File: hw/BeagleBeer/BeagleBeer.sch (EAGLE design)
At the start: 104 parts, among them Q10 BSS138, Q9 BSS138, U1 TEMPERATURE-SENSORUMAX8, U4 CAT24C256WI-GT3, U5 BEAGLEBONE_OUTLINEBEAGLEBEER

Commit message: BeagleBeer v2 Run ERCs and DRCs
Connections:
- new net N$12: JP2.20, U5.GPIO2_13
- new net N$13: JP2.21, U5.GPIO2_11
- new net N$20: JP1.4, U5.GPIO2_12
- new net N$21: JP1.3, U5.GPIO2_10
- net 3.3V: now also R15.2, R16.2, R22.2, R25.2
- net LED_FLOW_B_3P3: now also U2.A2
- net LED_FLOW_C_3P3: no longer JP2.20, U5.GPIO2_13
- net LED_FLOW_D_3P3: no longer JP2.21, U5.GPIO2_11
- net N$2: now also JP1.2, U5.GPIO2_8; no longer R22.2, R25.2
- net N$3: now also JP1.1, U5.GPIO2_6; no longer R15.2, R16.2
- net RELAY_A_3P3: no longer JP1.4, U5.GPIO2_12
- net RELAY_B_3P3: no longer JP1.3, U5.GPIO2_10
- net RELAY_C_3P3: no longer JP1.2, U5.GPIO2_8
- net RELAY_D_3P3: no longer JP1.1, U5.GPIO2_6
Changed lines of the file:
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@@
-</segment>
-</net>
-<net name="N$39" class="0">
-<segment>
-<wire x1="157.48" y1="154.94" x2="167.64" y2="154.94" width="0.1524" layer="91"/>
-<pinref part="JP2" gate="G$1" pin="16"/>
-<pinref part="U5" gate="G$1" pin="UART5_RTSN"/>
-</segment>
-</net>
-<net name="N$40" class="0">
-<segment>
-<wire x1="157.48" y1="152.4" x2="167.64" y2="152.4" width="0.1524" layer="91"/>
-<pinref part="JP2" gate="G$1" pin="17"/>
-<pinref part="U5" gate="G$1" pin="UART3_RTSN"/>
-</segment>
-</net>
-<net name="N$41" class="0">
-<segment>
-<wire x1="157.48" y1="149.86" x2="167.64" y2="149.86" width="0.1524" layer="91"/>
-<pinref part="JP2" gate="G$1" pin="18"/>
-<pinref part="U5" gate="G$1" pin="UART3_CTSN"/>
-</segment>
-</net>
-<net name="N$45" class="0">
-<segment>
-<wire x1="157.48" y1="139.7" x2="167.64" y2="139.7" width="0.1524" layer="91"/>
-<pinref part="JP2" gate="G$1" pin="22"/>
-<pinref part="U5" gate="G$1" pin="GPIO2_9"/>
-</segment>
-</net>
-<net name="N$46" class="0">
-<segment>
-<wire x1="157.48" y1="137.16" x2="167.64" y2="137.16" width="0.1524" layer="91"/>
-<pinref part="JP2" gate="G$1" pin="23"/>
-<pinref part="U5" gate="G$1" pin="GPIO2_7"/>
 </segment>
 </net>
@@
 <pinref part="R17" gate="G$1" pin="2"/>
 <wire x1="276.86" y1="254" x2="276.86" y2="256.54" width="0.1524" layer="91"/>
+<junction x="276.86" y="256.54"/>
 </segment>
 <segment>
@@
 <pinref part="R39" gate="G$1" pin="2"/>
 <wire x1="276.86" y1="213.36" x2="276.86" y2="215.9" width="0.1524" layer="91"/>
+<junction x="276.86" y="215.9"/>
 </segment>
 </net>
@@
 </segment>
 <segment>
-<wire x1="101.6" y1="137.16" x2="91.44" y2="137.16" width="0.1524" layer="91"/>
-<pinref part="JP1" gate="G$1" pin="1"/>
-<pinref part="U5" gate="G$1" pin="GPIO2_6"/>
-</segment>
-<segment>
 <wire x1="200.66" y1="162.56" x2="167.64" y2="162.56" width="0.1524" layer="91"/>
 <label x="175.26" y="162.56" size="1.778" layer="95"/>
@@
 </segment>
 <segment>
-<wire x1="101.6" y1="139.7" x2="91.44" y2="139.7" width="0.1524" layer="91"/>
-<pinref part="JP1" gate="G$1" pin="2"/>
-<pinref part="U5" gate="G$1" pin="GPIO2_8"/>
-</segment>
-<segment>
 <wire x1="200.66" y1="165.1" x2="167.64" y2="165.1" width="0.1524" layer="91"/>
 <label x="175.26" y="165.1" size="1.778" layer="95"/>
@@
 </segment>
 <segment>
-<wire x1="101.6" y1="142.24" x2="91.44" y2="142.24" width="0.1524" layer="91"/>
-<pinref part="JP1" gate="G$1" pin="3"/>
-<pinref part="U5" gate="G$1" pin="GPIO2_10"/>
-</segment>
-<segment>
 <wire x1="200.66" y1="167.64" x2="167.64" y2="167.64" width="0.1524" layer="91"/>
 <label x="175.26" y="167.64" size="1.778" layer="95"/>
@@
 <wire x1="284.48" y1="78.74" x2="264.16" y2="78.74" width="0.1524" layer="91"/>
 <label x="264.16" y="78.74" size="1.778" layer="95"/>
-</segment>
-<segment>
-<wire x1="101.6" y1="144.78" x2="91.44" y2="144.78" width="0.1524" layer="91"/>
-<pinref part="JP1" gate="G$1" pin="4"/>
-<pinref part="U5" gate="G$1" pin="GPIO2_12"/>
 </segment>
 <segment>
@@
 <wire x1="276.86" y1="190.5" x2="251.46" y2="190.5" width="0.1524" layer="91"/>
 <label x="254" y="190.5" size="1.778" layer="95"/>
+<junction x="276.86" y="198.12"/>
 </segment>
 </net>
@@
 <wire x1="276.86" y1="233.68" x2="251.46" y2="233.68" width="0.1524" layer="91"/>
 <label x="254" y="233.68" size="1.778" layer="95"/>
+<junction x="276.86" y="238.76"/>
 </segment>
 </net>
@@
 <segment>
 <label x="251.46" y="144.78" size="1.778" layer="95"/>
-<wire x1="251.46" y1="144.78" x2="281.94" y2="144.78" width="0.1524" layer="91"/>
+<wire x1="251.46" y1="144.78" x2="279.4" y2="144.78" width="0.1524" layer="91"/>
+<pinref part="U2" gate="G$1" pin="A2"/>
 </segment>
 </net>
 <net name="LED_FLOW_C_3P3" class="0">
-<segment>
-<pinref part="JP2" gate="G$1" pin="20"/>
-<pinref part="U5" gate="G$1" pin="GPIO2_13"/>
-<wire x1="167.64" y1="144.78" x2="157.48" y2="144.78" width="0.1524" layer="91"/>
-</segment>
 <segment>
 <wire x1="167.64" y1="160.02" x2="200.66" y2="160.02" width="0.1524" layer="91"/>
@@
 </net>
 <net name="LED_FLOW_D_3P3" class="0">
-<segment>
-<wire x1="157.48" y1="142.24" x2="167.64" y2="142.24" width="0.1524" layer="91"/>
-<pinref part="JP2" gate="G$1" pin="21"/>
-<pinref part="U5" gate="G$1" pin="GPIO2_11"/>
-</segment>
 <segment>
 <wire x1="167.64" y1="157.48" x2="200.66" y2="157.48" width="0.1524" layer="91"/>
@@
 </segment>
 </net>
-<net name="N$6" class="0">
-<segment>
-<wire x1="157.48" y1="147.32" x2="167.64" y2="147.32" width="0.1524" layer="91"/>
-<pinref part="JP2" gate="G$1" pin="19"/>
-<pinref part="U5" gate="G$1" pin="UART5_RXD"/>
-</segment>
-</net>
 <net name="LED_FLOW_A" class="0">
 <segment>
@@
 <wire x1="309.88" y1="190.5" x2="335.28" y2="190.5" width="0.1524" layer="91"/>
 <label x="317.5" y="190.5" size="1.778" layer="95"/>
+<junction x="309.88" y="198.12"/>
 </segment>
 </net>
@@
 <wire x1="314.96" y1="233.68" x2="337.82" y2="233.68" width="0.1524" layer="91"/>
 <label x="320.04" y="233.68" size="1.778" layer="95"/>
+<junction x="314.96" y="238.76"/>
+</segment>
+</net>
+<net name="N$2" class="0">
+<segment>
+<pinref part="U5" gate="G$1" pin="GPIO2_8"/>
+<pinref part="JP1" gate="G$1" pin="2"/>
+<wire x1="101.6" y1="139.7" x2="91.44" y2="139.7" width="0.1524" layer="91"/>
+</segment>
+</net>
+<net name="N$3" class="0">
+<segment>
+<pinref part="JP1" gate="G$1" pin="1"/>
+<pinref part="U5" gate="G$1" pin="GPIO2_6"/>
+<wire x1="91.44" y1="137.16" x2="101.6" y2="137.16" width="0.1524" layer="91"/>
+</segment>
+</net>
+<net name="N$6" class="0">
+<segment>
+<pinref part="U5" gate="G$1" pin="UART5_RTSN"/>
+<pinref part="JP2" gate="G$1" pin="16"/>
+<wire x1="157.48" y1="154.94" x2="167.64" y2="154.94" width="0.1524" layer="91"/>
+</segment>
+</net>
+<net name="N$8" class="0">
+<segment>
+<pinref part="U5" gate="G$1" pin="UART3_RTSN"/>
+<pinref part="JP2" gate="G$1" pin="17"/>
+<wire x1="157.48" y1="152.4" x2="167.64" y2="152.4" width="0.1524" layer="91"/>
+</segment>
+</net>
+<net name="N$9" class="0">
+<segment>
+<pinref part="U5" gate="G$1" pin="UART3_CTSN"/>
+<pinref part="JP2" gate="G$1" pin="18"/>
+<wire x1="157.48" y1="149.86" x2="167.64" y2="149.86" width="0.1524" layer="91"/>
+</segment>
+</net>
+<net name="N$11" class="0">
+<segment>
+<pinref part="U5" gate="G$1" pin="UART5_RXD"/>
+<pinref part="JP2" gate="G$1" pin="19"/>
+<wire x1="157.48" y1="147.32" x2="167.64" y2="147.32" width="0.1524" layer="91"/>
+</segment>
+</net>
+<net name="N$12" class="0">
+<segment>
+<pinref part="U5" gate="G$1" pin="GPIO2_13"/>
+<pinref part="JP2" gate="G$1" pin="20"/>
+<wire x1="157.48" y1="144.78" x2="167.64" y2="144.78" width="0.1524" layer="91"/>
+</segment>
+</net>
+<net name="N$13" class="0">
+<segment>
+<pinref part="U5" gate="G$1" pin="GPIO2_11"/>
+<pinref part="JP2" gate="G$1" pin="21"/>
+<wire x1="157.48" y1="142.24" x2="167.64" y2="142.24" width="0.1524" layer="91"/>
+</segment>
+</net>
+<net name="N$14" class="0">
+<segment>
+<pinref part="U5" gate="G$1" pin="GPIO2_9"/>
+<pinref part="JP2" gate="G$1" pin="22"/>
+<wire x1="157.48" y1="139.7" x2="167.64" y2="139.7" width="0.1524" layer="91"/>
+</segment>
+</net>
+<net name="N$15" class="0">
+<segment>
+<pinref part="U5" gate="G$1" pin="GPIO2_7"/>
+<pinref part="JP2" gate="G$1" pin="23"/>
+<wire x1="157.48" y1="137.16" x2="167.64" y2="137.16" width="0.1524" layer="91"/>
+</segment>
+</net>
+<net name="N$20" class="0">
+<segment>
+<pinref part="JP1" gate="G$1" pin="4"/>
+<pinref part="U5" gate="G$1" pin="GPIO2_12"/>
+<wire x1="91.44" y1="144.78" x2="101.6" y2="144.78" width="0.1524" layer="91"/>
+</segment>
+</net>
+<net name="N$21" class="0">
+<segment>
+<pinref part="JP1" gate="G$1" pin="3"/>
+<pinref part="U5" gate="G$1" pin="GPIO2_10"/>
+<wire x1="91.44" y1="142.24" x2="101.6" y2="142.24" width="0.1524" layer="91"/>
 </segment>
 </net>
@@
 <net name="3.3V" class="0">
 <segment>
+<pinref part="U$30" gate="G$1" pin="3.3V"/>
 <pinref part="C2" gate="G$1" pin="1"/>
-<pinref part="U$30" gate="G$1" pin="3.3V"/>
-<wire x1="22.86" y1="30.48" x2="22.86" y2="33.02" width="0.1524" layer="91"/>
-<wire x1="22.86" y1="33.02" x2="22.86" y2="38.1" width="0.1524" layer="91"/>
-<wire x1="22.86" y1="33.02" x2="22.86" y2="40.64" width="0.1524" layer="91"/>
-</segment>
-<segment>
-<pinref part="U$5" gate="G$1" pin="3.3V"/>
-<wire x1="134.62" y1="243.84" x2="134.62" y2="248.92" width="0.1524" layer="91"/>
-<wire x1="134.62" y1="243.84" x2="134.62" y2="251.46" width="0.1524" layer="91"/>
-</segment>
-<segment>
-<pinref part="U$7" gate="G$1" pin="3.3V"/>
-<wire x1="185.42" y1="243.84" x2="185.42" y2="248.92" width="0.1524" layer="91"/>
-<wire x1="185.42" y1="243.84" x2="185.42" y2="251.46" width="0.1524" layer="91"/>
-</segment>
-</net>
-<net name="N$2" class="0">
+<wire x1="22.86" y1="30.48" x2="22.86" y2="38.1" width="0.1524" layer="91"/>
+</segment>
 <segment>
 <wire x1="119.38" y1="238.76" x2="134.62" y2="238.76" width="0.1524" layer="91"/>
-<wire x1="134.62" y1="238.76" x2="134.62" y2="246.38" width="0.1524" layer="91"/>
 <wire x1="119.38" y1="228.6" x2="134.62" y2="228.6" width="0.1524" layer="91"/>
 <wire x1="134.62" y1="228.6" x2="134.62" y2="238.76" width="0.1524" layer="91"/>
@@
 <pinref part="R22" gate="G$1" pin="2"/>
 <pinref part="R25" gate="G$1" pin="2"/>
-</segment>
-</net>
-<net name="N$3" class="0">
-<segment>
-<wire x1="185.42" y1="238.76" x2="185.42" y2="243.84" width="0.1524" layer="91"/>
+<pinref part="U$5" gate="G$1" pin="3.3V"/>
+<wire x1="134.62" y1="238.76" x2="134.62" y2="248.92" width="0.1524" layer="91"/>
+</segment>
+<segment>
 <wire x1="170.18" y1="238.76" x2="185.42" y2="238.76" width="0.1524" layer="91"/>
 <wire x1="170.18" y1="228.6" x2="185.42" y2="228.6" width="0.1524" layer="91"/>
@@
 <pinref part="R16" gate="G$1" pin="2"/>
 <junction x="185.42" y="238.76"/>
-</segment>
-</net>
+<pinref part="U$7" gate="G$1" pin="3.3V"/>
+<wire x1="185.42" y1="238.76" x2="185.42" y2="248.92" width="0.1524" layer="91"/>
+</segment>
+</net>

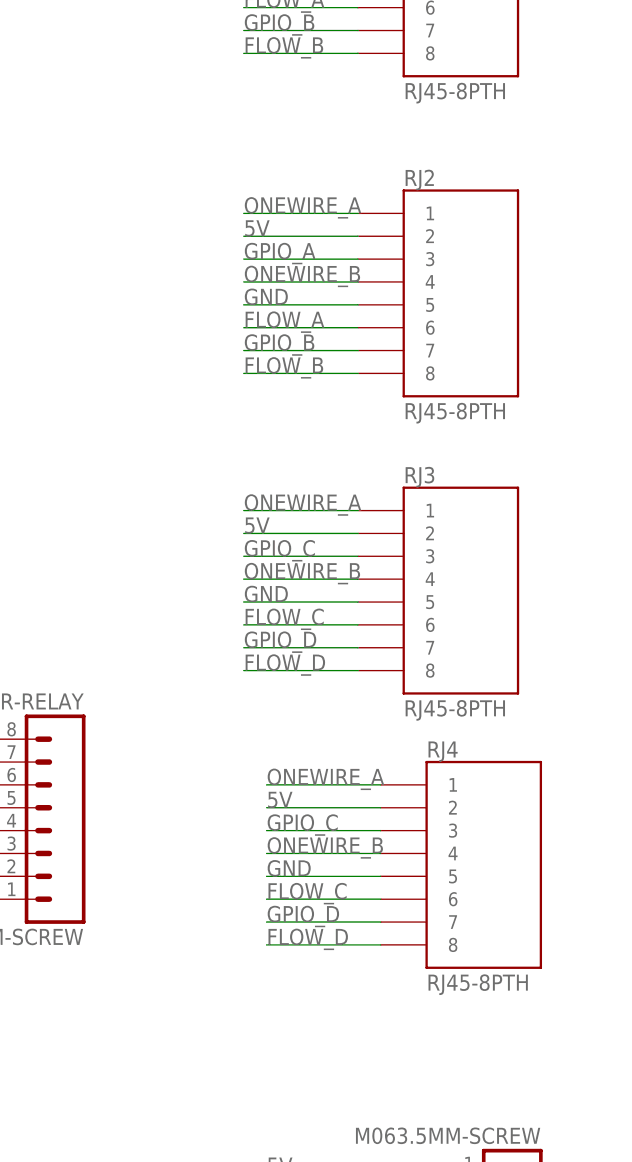
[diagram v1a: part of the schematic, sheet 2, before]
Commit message: Remove redundant RJ45 connectors on BeagleBeer
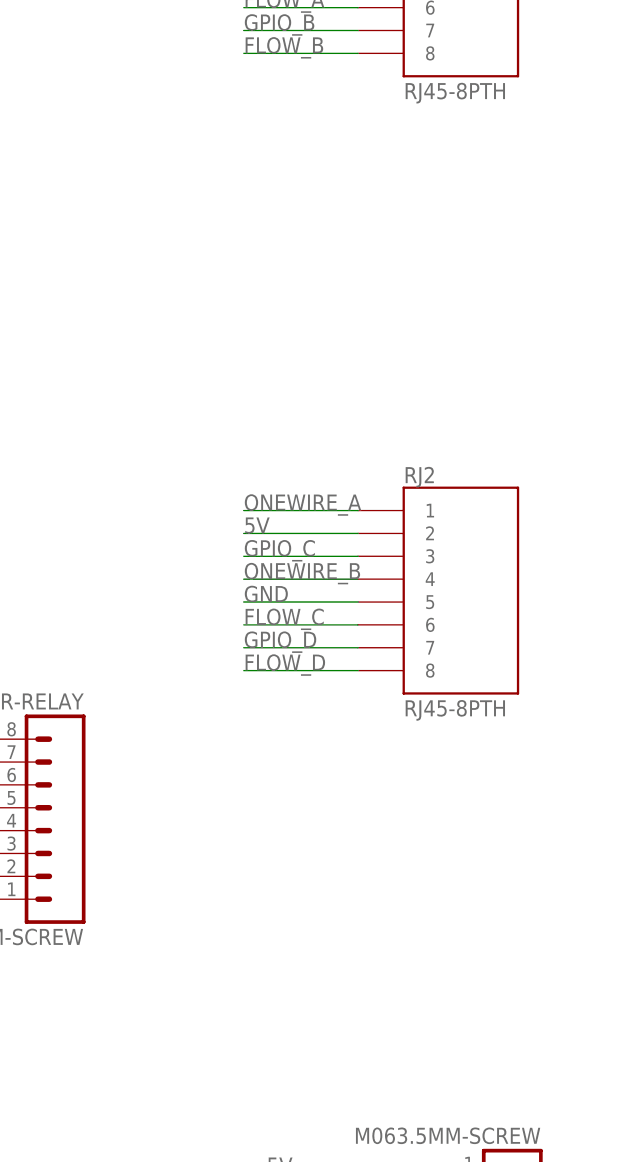
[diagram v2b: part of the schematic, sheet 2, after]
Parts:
- removed RJ3, RJ4: RJ45-8PTH, SparkFun:RJ45-8PTH
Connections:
- net 5V: no longer RJ3.2, RJ4.2
- net FLOW_A: no longer RJ2.6
- net FLOW_B: no longer RJ2.8
- net FLOW_C: now also RJ2.6; no longer RJ3.6, RJ4.6
- net FLOW_D: now also RJ2.8; no longer RJ3.8, RJ4.8
- net GND: no longer RJ3.5, RJ4.5
- net GPIO_A: no longer RJ2.3
- net GPIO_B: no longer RJ2.7
- net GPIO_C: now also RJ2.3; no longer RJ3.3, RJ4.3
- net GPIO_D: now also RJ2.7; no longer RJ3.7, RJ4.7
- net ONEWIRE_A: no longer RJ3.1, RJ4.1
- net ONEWIRE_B: no longer RJ3.4, RJ4.4
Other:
- moved on the sheet: RJ2
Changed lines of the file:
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@@
 <part name="RELAY_C" library="SparkFun" deviceset="RELAY" device="PTH"/>
 <part name="RELAY_D" library="SparkFun" deviceset="RELAY" device="PTH"/>
-<part name="RJ2" library="SparkFun" deviceset="RJ45-8" device="PTH"/>
 <part name="GND12" library="SparkFun" deviceset="GND" device=""/>
 <part name="U$37" library="SparkFun" deviceset="5V" device=""/>
@@
 <part name="U$40" library="microbuilder" deviceset="3.3V" device=""/>
 <part name="TEST_D" library="SparkFun-20100412" deviceset="JUMPER-2" device="PTH"/>
-<part name="RJ3" library="SparkFun" deviceset="RJ45-8" device="PTH"/>
+<part name="RJ2" library="SparkFun" deviceset="RJ45-8" device="PTH"/>
 <part name="TEST_C" library="SparkFun-20100412" deviceset="JUMPER-2" device="PTH"/>
-<part name="RJ4" library="SparkFun" deviceset="RJ45-8" device="PTH"/>
 <part name="U$16" library="SparkFun" deviceset="5V" device=""/>
 <part name="U$29" library="SparkFun" deviceset="5V" device=""/>
@@
 <instance part="RELAY_C" gate="G$1" x="271.78" y="109.22"/>
 <instance part="RELAY_D" gate="G$1" x="271.78" y="43.18"/>
-<instance part="RJ2" gate="G$1" x="363.22" y="198.12"/>
 <instance part="GND12" gate="1" x="25.4" y="73.66"/>
 <instance part="U$37" gate="G$1" x="167.64" y="160.02"/>
@@
 <instance part="LED9" gate="G$1" x="111.76" y="83.82" rot="R90"/>
 <instance part="TEST_D" gate="A" x="365.76" y="48.26" rot="R270"/>
-<instance part="RJ3" gate="G$1" x="363.22" y="165.1"/>
+<instance part="RJ2" gate="G$1" x="363.22" y="165.1"/>
 <instance part="TEST_C" gate="A" x="365.76" y="55.88" rot="R270"/>
-<instance part="RJ4" gate="G$1" x="365.76" y="134.62"/>
 <instance part="U$16" gate="G$1" x="134.62" y="215.9"/>
 <instance part="U$29" gate="G$1" x="33.02" y="99.06"/>
@@
 </segment>
 <segment>
-<wire x1="350.52" y1="195.58" x2="337.82" y2="195.58" width="0.1524" layer="91"/>
-<label x="337.82" y="195.58" size="1.778" layer="95"/>
-<pinref part="RJ2" gate="G$1" pin="6"/>
-</segment>
-<segment>
 <wire x1="109.22" y1="238.76" x2="93.98" y2="238.76" width="0.1524" layer="91"/>
 <label x="93.98" y="238.76" size="1.778" layer="95"/>
@@
 </segment>
 <segment>
-<wire x1="350.52" y1="190.5" x2="337.82" y2="190.5" width="0.1524" layer="91"/>
-<label x="337.82" y="190.5" size="1.778" layer="95"/>
-<pinref part="RJ2" gate="G$1" pin="8"/>
-</segment>
-<segment>
 <wire x1="109.22" y1="228.6" x2="93.98" y2="228.6" width="0.1524" layer="91"/>
 <label x="93.98" y="228.6" size="1.778" layer="95"/>
@@
 <net name="GPIO_C" class="0">
 <segment>
-<pinref part="RJ3" gate="G$1" pin="3"/>
+<pinref part="RJ2" gate="G$1" pin="3"/>
 <wire x1="350.52" y1="170.18" x2="337.82" y2="170.18" width="0.1524" layer="91"/>
 <label x="337.82" y="170.18" size="1.778" layer="95"/>
-</segment>
-<segment>
-<pinref part="RJ4" gate="G$1" pin="3"/>
-<wire x1="353.06" y1="139.7" x2="340.36" y2="139.7" width="0.1524" layer="91"/>
-<label x="340.36" y="139.7" size="1.778" layer="95"/>
 </segment>
 </net>
@@
 </segment>
 <segment>
-<wire x1="350.52" y1="208.28" x2="337.82" y2="208.28" width="0.1524" layer="91"/>
-<label x="337.82" y="208.28" size="1.778" layer="95"/>
-<pinref part="RJ2" gate="G$1" pin="1"/>
-</segment>
-<segment>
 <wire x1="55.88" y1="83.82" x2="73.66" y2="83.82" width="0.1524" layer="91"/>
 <label x="58.42" y="83.82" size="1.778" layer="95"/>
@@
 </segment>
 <segment>
-<pinref part="RJ3" gate="G$1" pin="1"/>
+<pinref part="RJ2" gate="G$1" pin="1"/>
 <wire x1="350.52" y1="175.26" x2="337.82" y2="175.26" width="0.1524" layer="91"/>
 <label x="337.82" y="175.26" size="1.778" layer="95"/>
-</segment>
-<segment>
-<pinref part="RJ4" gate="G$1" pin="1"/>
-<wire x1="353.06" y1="144.78" x2="340.36" y2="144.78" width="0.1524" layer="91"/>
-<label x="340.36" y="144.78" size="1.778" layer="95"/>
 </segment>
 </net>
@@
 </segment>
 <segment>
-<wire x1="350.52" y1="200.66" x2="337.82" y2="200.66" width="0.1524" layer="91"/>
-<label x="337.82" y="200.66" size="1.778" layer="95"/>
-<pinref part="RJ2" gate="G$1" pin="4"/>
-</segment>
-<segment>
 <wire x1="109.22" y1="200.66" x2="93.98" y2="200.66" width="0.1524" layer="91"/>
 <label x="93.98" y="200.66" size="1.778" layer="95"/>
@@
 <segment>
 <label x="337.82" y="167.64" size="1.778" layer="95"/>
-<pinref part="RJ3" gate="G$1" pin="4"/>
+<pinref part="RJ2" gate="G$1" pin="4"/>
 <wire x1="350.52" y1="167.64" x2="337.82" y2="167.64" width="0.1524" layer="91"/>
-</segment>
-<segment>
-<label x="340.36" y="137.16" size="1.778" layer="95"/>
-<pinref part="RJ4" gate="G$1" pin="4"/>
-<wire x1="353.06" y1="137.16" x2="340.36" y2="137.16" width="0.1524" layer="91"/>
 </segment>
 </net>
@@
 <pinref part="RJ1" gate="G$1" pin="3"/>
 </segment>
-<segment>
-<wire x1="350.52" y1="203.2" x2="337.82" y2="203.2" width="0.1524" layer="91"/>
-<label x="337.82" y="203.2" size="1.778" layer="95"/>
-<pinref part="RJ2" gate="G$1" pin="3"/>
-</segment>
 </net>
 <net name="GPIO_B" class="0">
@@
 <label x="337.82" y="228.6" size="1.778" layer="95"/>
 <pinref part="RJ1" gate="G$1" pin="7"/>
-</segment>
-<segment>
-<wire x1="350.52" y1="193.04" x2="337.82" y2="193.04" width="0.1524" layer="91"/>
-<label x="337.82" y="193.04" size="1.778" layer="95"/>
-<pinref part="RJ2" gate="G$1" pin="7"/>
 </segment>
 </net>
@@
 </segment>
 <segment>
-<wire x1="350.52" y1="198.12" x2="337.82" y2="198.12" width="0.1524" layer="91"/>
-<label x="337.82" y="198.12" size="1.778" layer="95"/>
-<pinref part="RJ2" gate="G$1" pin="5"/>
-</segment>
-<segment>
 <wire x1="38.1" y1="81.28" x2="25.4" y2="81.28" width="0.1524" layer="91"/>
 <wire x1="25.4" y1="81.28" x2="25.4" y2="76.2" width="0.1524" layer="91"/>
@@
 <wire x1="350.52" y1="165.1" x2="337.82" y2="165.1" width="0.1524" layer="91"/>
 <label x="337.82" y="165.1" size="1.778" layer="95"/>
-<pinref part="RJ3" gate="G$1" pin="5"/>
-</segment>
-<segment>
-<wire x1="353.06" y1="134.62" x2="340.36" y2="134.62" width="0.1524" layer="91"/>
-<label x="340.36" y="134.62" size="1.778" layer="95"/>
-<pinref part="RJ4" gate="G$1" pin="5"/>
+<pinref part="RJ2" gate="G$1" pin="5"/>
 </segment>
 <segment>
@@
 </segment>
 <segment>
-<wire x1="350.52" y1="205.74" x2="337.82" y2="205.74" width="0.1524" layer="91"/>
-<label x="337.82" y="205.74" size="1.778" layer="95"/>
-<pinref part="RJ2" gate="G$1" pin="2"/>
-</segment>
-<segment>
 <wire x1="238.76" y1="243.84" x2="238.76" y2="241.3" width="0.1524" layer="91"/>
 <pinref part="U$17" gate="G$1" pin="5V"/>
@@
 <wire x1="350.52" y1="172.72" x2="337.82" y2="172.72" width="0.1524" layer="91"/>
 <label x="337.82" y="172.72" size="1.778" layer="95"/>
-<pinref part="RJ3" gate="G$1" pin="2"/>
-</segment>
-<segment>
-<wire x1="353.06" y1="142.24" x2="340.36" y2="142.24" width="0.1524" layer="91"/>
-<label x="340.36" y="142.24" size="1.778" layer="95"/>
-<pinref part="RJ4" gate="G$1" pin="2"/>
+<pinref part="RJ2" gate="G$1" pin="2"/>
 </segment>
 <segment>
@@
 <net name="GPIO_D" class="0">
 <segment>
-<pinref part="RJ3" gate="G$1" pin="7"/>
+<pinref part="RJ2" gate="G$1" pin="7"/>
 <wire x1="350.52" y1="160.02" x2="337.82" y2="160.02" width="0.1524" layer="91"/>
 <label x="337.82" y="160.02" size="1.778" layer="95"/>
-</segment>
-<segment>
-<pinref part="RJ4" gate="G$1" pin="7"/>
-<wire x1="353.06" y1="129.54" x2="340.36" y2="129.54" width="0.1524" layer="91"/>
-<label x="340.36" y="129.54" size="1.778" layer="95"/>
 </segment>
 </net>
@@
 </segment>
 <segment>
-<pinref part="RJ3" gate="G$1" pin="6"/>
+<pinref part="RJ2" gate="G$1" pin="6"/>
 <wire x1="350.52" y1="162.56" x2="337.82" y2="162.56" width="0.1524" layer="91"/>
 <label x="337.82" y="162.56" size="1.778" layer="95"/>
-</segment>
-<segment>
-<pinref part="RJ4" gate="G$1" pin="6"/>
-<wire x1="353.06" y1="132.08" x2="340.36" y2="132.08" width="0.1524" layer="91"/>
-<label x="340.36" y="132.08" size="1.778" layer="95"/>
 </segment>
 </net>
@@
 </segment>
 <segment>
-<pinref part="RJ3" gate="G$1" pin="8"/>
+<pinref part="RJ2" gate="G$1" pin="8"/>
 <wire x1="350.52" y1="157.48" x2="337.82" y2="157.48" width="0.1524" layer="91"/>
 <label x="337.82" y="157.48" size="1.778" layer="95"/>
 </segment>
-<segment>
-<pinref part="RJ4" gate="G$1" pin="8"/>
-<wire x1="353.06" y1="127" x2="340.36" y2="127" width="0.1524" layer="91"/>
-<label x="340.36" y="127" size="1.778" layer="95"/>
-</segment>
-</net>
+</net>
